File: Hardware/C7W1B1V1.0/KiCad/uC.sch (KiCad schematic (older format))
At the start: 7 parts, among them U1 STM32L082KBUx

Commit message: początkowy schemat
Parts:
- removed U1: STM32L082KBUx, Package_DFN_QFN:QFN-32-1EP_5x5mm_P0.5mm_EP3.45x3.45mm, symbol MCU_ST_STM32L0:STM32L082KBUx
- added C19: 100n/16V/X5R, Capacitor_SMD:C_0402_1005Metric, symbol Device:C
- added C5, C6: 8p/16V/C0G, Capacitor_SMD:C_0402_1005Metric, symbol Device:C
- added U1: STM32L083CZTx, Package_QFP:LQFP-48_7x7mm_P0.5mm, symbol MCU_ST_STM32L0:STM32L083CZTx
- added Y1: 830106545501, Crystal:Crystal_SMD_2012-2Pin_2.0x1.2mm, symbol Device:Crystal
- gave numbers to parts that had none: 2
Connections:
- net labels added: 5V_EN, 5V_TEST, BATT, E_INC_BUSY, E_INC_CS, E_INC_DC, E_INC_RST, MOSI, PMS_RST, PMS_TX, SCK, SCL, SDA, ~CHRG_STATUS
- wire segments 22 -> 42
- no-connect marks 0 -> 2
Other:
- moved on the sheet: C1, C2, C3, C4, R1, R2

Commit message: Dodano projekt Cube
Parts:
- renumbered C5 to C1, C6 to C2, C19 to C3, C1 to C4, C2 to C5, C3 to C6, C4 to C7, R2 to R1, R1 to R2
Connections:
- net E_INC_DC: now also U1.21 (PB10); no longer U1.39 (PB3)
- net PMS_RST: now also U1.29 (PA8)
- net PMS_TX: now also U1.31 (PA10)
- net ~CHRG_STATUS: now also U1.2 (PC13)
- net ~FLASH_CS: now reaches U1.13 (PA3)
- net ~FRAM_CS: now reaches U1.14 (PA4)
- net MISO: now reaches U1.17 (PA7)
- net PMS_SET: now reaches U1.28 (PB15)
- net PMS_RX: now reaches U1.30 (PA9)
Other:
- moved on the sheet: R1
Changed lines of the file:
@@
 	7850 950  7500 950
 $Comp
-L Device:C C4
+L Device:C C7
 U 1 1 672E6E58
 P 7500 1100
-F 0 "C4" V 7750 1050 50  0000 L CNN
+F 0 "C7" V 7750 1050 50  0000 L CNN
 F 1 "100n/16V/X5R" V 7650 650 50  0000 L CNN
 F 2 "Capacitor_SMD:C_0402_1005Metric" H 7538 950 50  0001 C CNN
@@
 	7850 950  7850 650
 $Comp
-L power:+3V3 #PWR0101
+L power:+3V3 #PWR06
 U 1 1 672E8774
 P 7850 650
-F 0 "#PWR0101" H 7850 500 50  0001 C CNN
+F 0 "#PWR06" H 7850 500 50  0001 C CNN
 F 1 "+3V3" H 7865 823 50  0000 C CNN
 F 2 "" H 7850 650 50  0001 C CNN
@@
 $EndComp
 $Comp
-L power:GND #PWR0102
+L power:GND #PWR02
 U 1 1 672E8F61
 P 6300 1250
-F 0 "#PWR0102" H 6300 1000 50  0001 C CNN
+F 0 "#PWR02" H 6300 1000 50  0001 C CNN
 F 1 "GND" H 6305 1077 50  0000 C CNN
 F 2 "" H 6300 1250 50  0001 C CNN
@@
 $EndComp
 $Comp
-L Device:C C3
+L Device:C C6
 U 1 1 672EA200
 P 7100 1100
-F 0 "C3" V 7350 1050 50  0000 L CNN
+F 0 "C6" V 7350 1050 50  0000 L CNN
 F 1 "100n/16V/X5R" V 7250 650 50  0000 L CNN
 F 2 "Capacitor_SMD:C_0402_1005Metric" H 7138 950 50  0001 C CNN
@@
 $EndComp
 $Comp
-L Device:C C2
+L Device:C C5
 U 1 1 672EA6BA
 P 6700 1100
-F 0 "C2" V 6950 1050 50  0000 L CNN
+F 0 "C5" V 6950 1050 50  0000 L CNN
 F 1 "100n/16V/X5R" V 6850 650 50  0000 L CNN
 F 2 "Capacitor_SMD:C_0402_1005Metric" H 6738 950 50  0001 C CNN
@@
 	7100 1250 6700 1250
 $Comp
-L Device:R R1
+L Device:R R2
 U 1 1 672EB48B
 P 6800 2000
-F 0 "R1" H 6870 2046 50  0000 L CNN
+F 0 "R2" H 6870 2046 50  0000 L CNN
 F 1 "10k/5%/0.063W" H 6870 1955 50  0000 L CNN
 F 2 "Resistor_SMD:R_0402_1005Metric" V 6730 2000 50  0001 C CNN
@@
 	6800 2200 6800 2150
 $Comp
-L power:+3V3 #PWR0103
+L power:+3V3 #PWR04
 U 1 1 672EC2CA
 P 6800 1850
-F 0 "#PWR0103" H 6800 1700 50  0001 C CNN
+F 0 "#PWR04" H 6800 1700 50  0001 C CNN
 F 1 "+3V3" H 6815 2023 50  0000 C CNN
 F 2 "" H 6800 1850 50  0001 C CNN
@@
 $EndComp
 $Comp
-L Device:R R2
+L Device:R R1
 U 1 1 672ECC6C
-P 6800 2650
-F 0 "R2" H 6870 2696 50  0000 L CNN
-F 1 "10k/5%/0.063W" V 6700 2600 50  0000 L CNN
-F 2 "Resistor_SMD:R_0402_1005Metric" V 6730 2650 50  0001 C CNN
-F 3 "~" H 6800 2650 50  0001 C CNN
-	1    6800 2650
-	1    0    0    -1
-$EndComp
-Wire Wire Line
-	7150 2400 6800 2400
-Wire Wire Line
-	6800 2400 6800 2500
-$Comp
-L power:GND #PWR0104
+P 6600 2500
+F 0 "R1" H 6670 2546 50  0000 L CNN
+F 1 "10k/5%/0.063W" V 6500 2450 50  0000 L CNN
+F 2 "Resistor_SMD:R_0402_1005Metric" V 6530 2500 50  0001 C CNN
+F 3 "~" H 6600 2500 50  0001 C CNN
+	1    6600 2500
+	1    0    0    -1
+$EndComp
+$Comp
+L power:GND #PWR03
 U 1 1 672ED76C
-P 6800 2800
-F 0 "#PWR0104" H 6800 2550 50  0001 C CNN
-F 1 "GND" H 6805 2627 50  0000 C CNN
-F 2 "" H 6800 2800 50  0001 C CNN
-F 3 "" H 6800 2800 50  0001 C CNN
-	1    6800 2800
-	1    0    0    -1
-$EndComp
-$Comp
-L power:GND #PWR0105
+P 6600 2650
+F 0 "#PWR03" H 6600 2400 50  0001 C CNN
+F 1 "GND" H 6605 2477 50  0000 C CNN
+F 2 "" H 6600 2650 50  0001 C CNN
+F 3 "" H 6600 2650 50  0001 C CNN
+	1    6600 2650
+	1    0    0    -1
+$EndComp
+$Comp
+L power:GND #PWR05
 U 1 1 672EDDA5
 P 7800 5100
-F 0 "#PWR0105" H 7800 4850 50  0001 C CNN
+F 0 "#PWR05" H 7800 4850 50  0001 C CNN
 F 1 "GND" H 7805 4927 50  0000 C CNN
 F 2 "" H 7800 5100 50  0001 C CNN
@@
 Text GLabel 7150 3400 0    50   Output ~ 0
 E_INC_RST
-Text GLabel 7150 3600 0    50   Output ~ 0
+Text GLabel 7150 4300 0    50   Output ~ 0
 E_INC_DC
-Text GLabel 4450 5100 2    50   Input ~ 0
+Text GLabel 8450 4100 2    50   Output ~ 0
 PMS_RST
-Text GLabel 4750 5000 0    50   Output ~ 0
+Text GLabel 8450 4300 2    50   Input ~ 0
 PMS_TX
 Text GLabel 7150 4000 0    50   BiDi ~ 0
@@
 	6700 950  6300 950
 $Comp
-L Device:C C1
+L Device:C C4
 U 1 1 672EA9E3
 P 6300 1100
-F 0 "C1" V 6550 1050 50  0000 L CNN
+F 0 "C4" V 6550 1050 50  0000 L CNN
 F 1 "100n/16V/X5R" V 6450 650 50  0000 L CNN
 F 2 "Capacitor_SMD:C_0402_1005Metric" H 6338 950 50  0001 C CNN
@@
 $EndComp
 $Comp
-L Device:C C19
+L Device:C C3
 U 1 1 67353EFC
 P 5900 1100
-F 0 "C19" V 6150 1050 50  0000 L CNN
+F 0 "C3" V 6150 1050 50  0000 L CNN
 F 1 "100n/16V/X5R" V 6050 650 50  0000 L CNN
 F 2 "Capacitor_SMD:C_0402_1005Metric" H 5938 950 50  0001 C CNN
@@
 	6000 2850 6550 2850
 $Comp
-L power:GND #PWR0106
+L power:GND #PWR01
 U 1 1 672FCAB2
 P 5100 3200
-F 0 "#PWR0106" H 5100 2950 50  0001 C CNN
+F 0 "#PWR01" H 5100 2950 50  0001 C CNN
 F 1 "GND" H 5105 3027 50  0000 C CNN
 F 2 "" H 5100 3200 50  0001 C CNN
@@
 	6000 3150 5700 3150
 $Comp
-L Device:C C6
+L Device:C C2
 U 1 1 672F9DE8
 P 5550 3150
-F 0 "C6" V 5600 3200 50  0000 L CNN
+F 0 "C2" V 5600 3200 50  0000 L CNN
 F 1 "8p/16V/C0G" V 5700 2900 50  0000 L CNN
 F 2 "Capacitor_SMD:C_0402_1005Metric" H 5588 3000 50  0001 C CNN
@@
 $EndComp
 $Comp
-L Device:C C5
+L Device:C C1
 U 1 1 672F967E
 P 5550 2850
-F 0 "C5" V 5600 2900 50  0000 L CNN
+F 0 "C1" V 5600 2900 50  0000 L CNN
 F 1 "8p/16V/C0G" V 5700 2600 50  0000 L CNN
 F 2 "Capacitor_SMD:C_0402_1005Metric" H 5588 2700 50  0001 C CNN
@@
 Text GLabel 8450 3300 2    50   Input ~ 0
 BATT
-Text GLabel 4850 6450 0    50   Output ~ 0
+Text GLabel 7150 2900 0    50   Input ~ 0
 ~CHRG_STATUS
+Text GLabel 8450 4200 2    50   Output ~ 0
+PMS_RX
+Text GLabel 7150 4800 0    50   Output ~ 0
+PMS_SET
+Wire Wire Line
+	6700 2400 6700 2350
+Wire Wire Line
+	6700 2350 6600 2350
+Wire Wire Line
+	6700 2400 7150 2400
+Text GLabel 8450 4000 2    50   Input ~ 0
+MISO
+Text GLabel 8450 3600 2    50   Input ~ 0
+~FLASH_CS
+Text GLabel 8450 3700 2    50   Input ~ 0
+~FRAM_CS
 $EndSCHEMATC

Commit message: Ukończono PCB. dodano pliki produkcyjne
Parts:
- added J5: Conn_01x07, Connector_PinSocket_2.54mm:PinSocket_1x07_P2.54mm_Vertical, symbol Connector_Generic:Conn_01x07
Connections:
- net 5V_EN: now also U1.11 (PA1); no longer U1.12 (PA2)
- net 5V_TEST: now also U1.12 (PA2); no longer U1.11 (PA1)
- net GND: now also J5.6 (Pin_6), J5.7 (Pin_7)
- net RST: now reaches R2.2, U1.7 (NRST)
- net RST: now also J5.1 (Pin_1)
- net USB_D-: now reaches U1.32 (PA11)
- net USB_D+: now reaches U1.33 (PA12)
- net SWDIO: now reaches U1.34 (PA13)
- net SWDIO: now also J5.5 (Pin_5)
- net SWCLK: now reaches U1.37 (PA14)
- net SWCLK: now also J5.4 (Pin_4)
- net TX: now reaches U1.39 (PB3)
- net TX: now also J5.3 (Pin_3)
- net RX: now reaches U1.40 (PB4)
- net RX: now also J5.2 (Pin_2)
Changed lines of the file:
@@
 NoConn ~ 7150 2600
 NoConn ~ 7150 2700
+Text GLabel 8450 3400 2    50   Output ~ 0
+5V_EN
 Text GLabel 8450 3500 2    50   Output ~ 0
-5V_EN
-Text GLabel 8450 3400 2    50   Output ~ 0
 5V_TEST
 Text GLabel 8450 3300 2    50   Input ~ 0
@@
 Text GLabel 8450 3700 2    50   Input ~ 0
 ~FRAM_CS
+Text GLabel 8450 4500 2    50   BiDi ~ 0
+USB_D+
+Text GLabel 8450 4400 2    50   BiDi ~ 0
+USB_D-
+Text GLabel 8450 4700 2    50   Input ~ 0
+SWCLK
+Text GLabel 8450 4600 2    50   BiDi ~ 0
+SWDIO
+Text GLabel 7150 3600 0    50   Output ~ 0
+TX
+Text GLabel 7150 3700 0    50   Input ~ 0
+RX
+Text GLabel 9950 1200 3    50   Input ~ 0
+TX
+Text GLabel 9850 1200 3    50   Output ~ 0
+RX
+Text GLabel 10050 1200 3    50   Output ~ 0
+SWCLK
+Text GLabel 10150 1200 3    50   BiDi ~ 0
+SWDIO
+Text GLabel 6800 2200 0    50   Input ~ 0
+RST
+Text GLabel 9750 1200 3    50   Output ~ 0
+RST
+$Comp
+L power:GND #PWR0108
+U 1 1 6753B37F
+P 10300 1300
+F 0 "#PWR0108" H 10300 1050 50  0001 C CNN
+F 1 "GND" H 10305 1127 50  0000 C CNN
+F 2 "" H 10300 1300 50  0001 C CNN
+F 3 "" H 10300 1300 50  0001 C CNN
+	1    10300 1300
+	1    0    0    -1
+$EndComp
+$Comp
+L Connector_Generic:Conn_01x07 J5
+U 1 1 6753EA67
+P 10050 1000
+F 0 "J5" V 10014 612 50  0000 R CNN
+F 1 "Conn_01x07" V 9923 612 50  0000 R CNN
+F 2 "Connector_PinSocket_2.54mm:PinSocket_1x07_P2.54mm_Vertical" H 10050 1000 50  0001 C CNN
+F 3 "~" H 10050 1000 50  0001 C CNN
+	1    10050 1000
+	0    -1   -1   0
+$EndComp
+Wire Wire Line
+	10250 1200 10300 1200
+Wire Wire Line
+	10300 1200 10300 1300
+Connection ~ 10300 1200
+Wire Wire Line
+	10300 1200 10350 1200
 $EndSCHEMATC

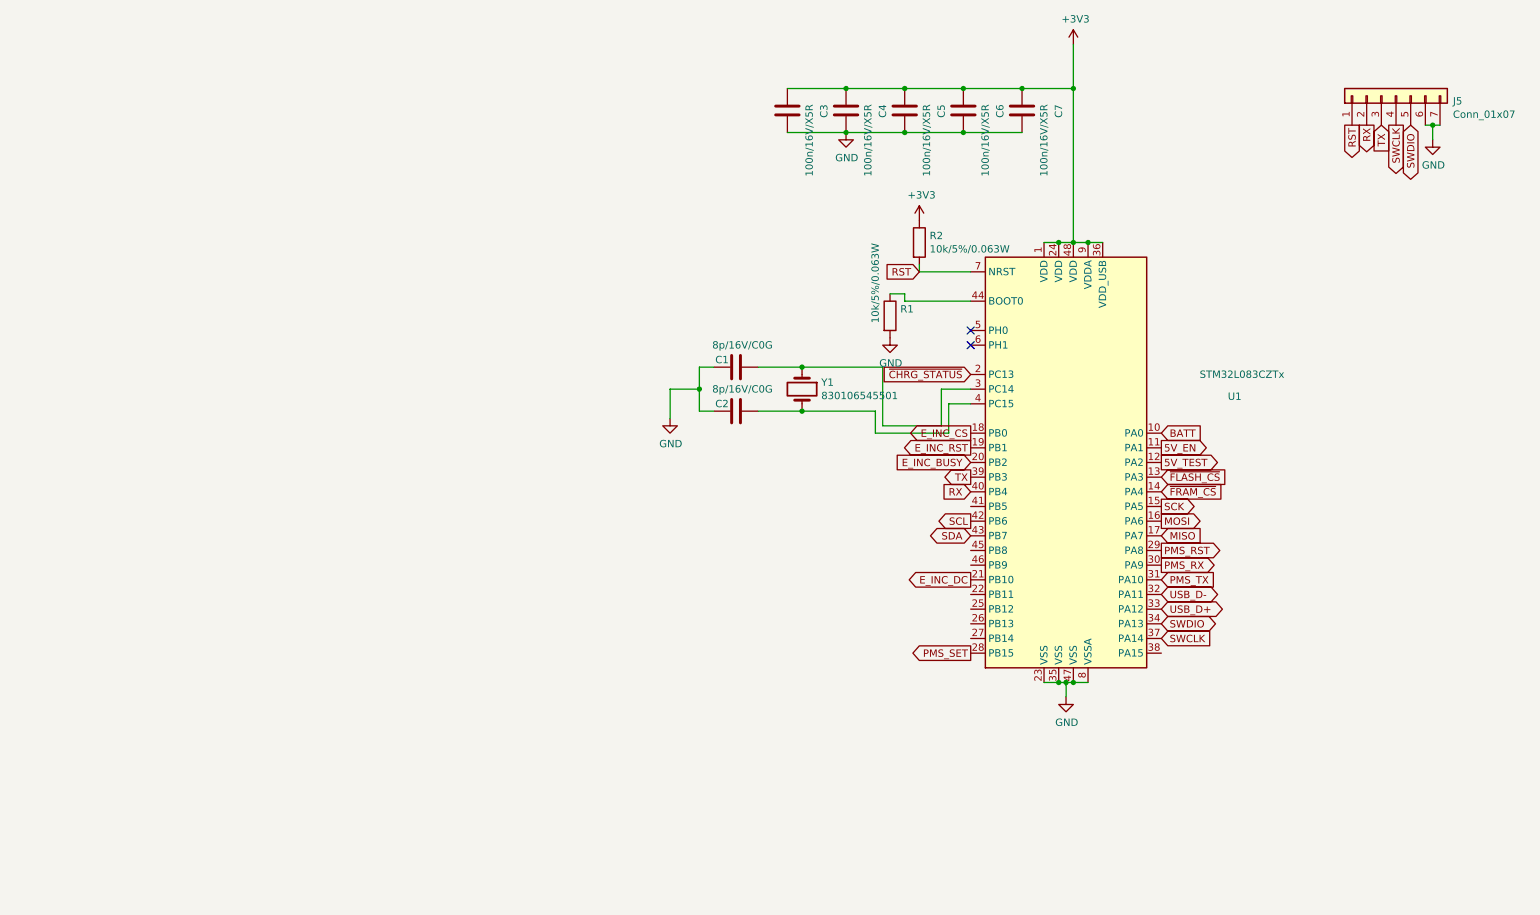
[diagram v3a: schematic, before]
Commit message: Zmieniono procesor na wersję LQFP-64
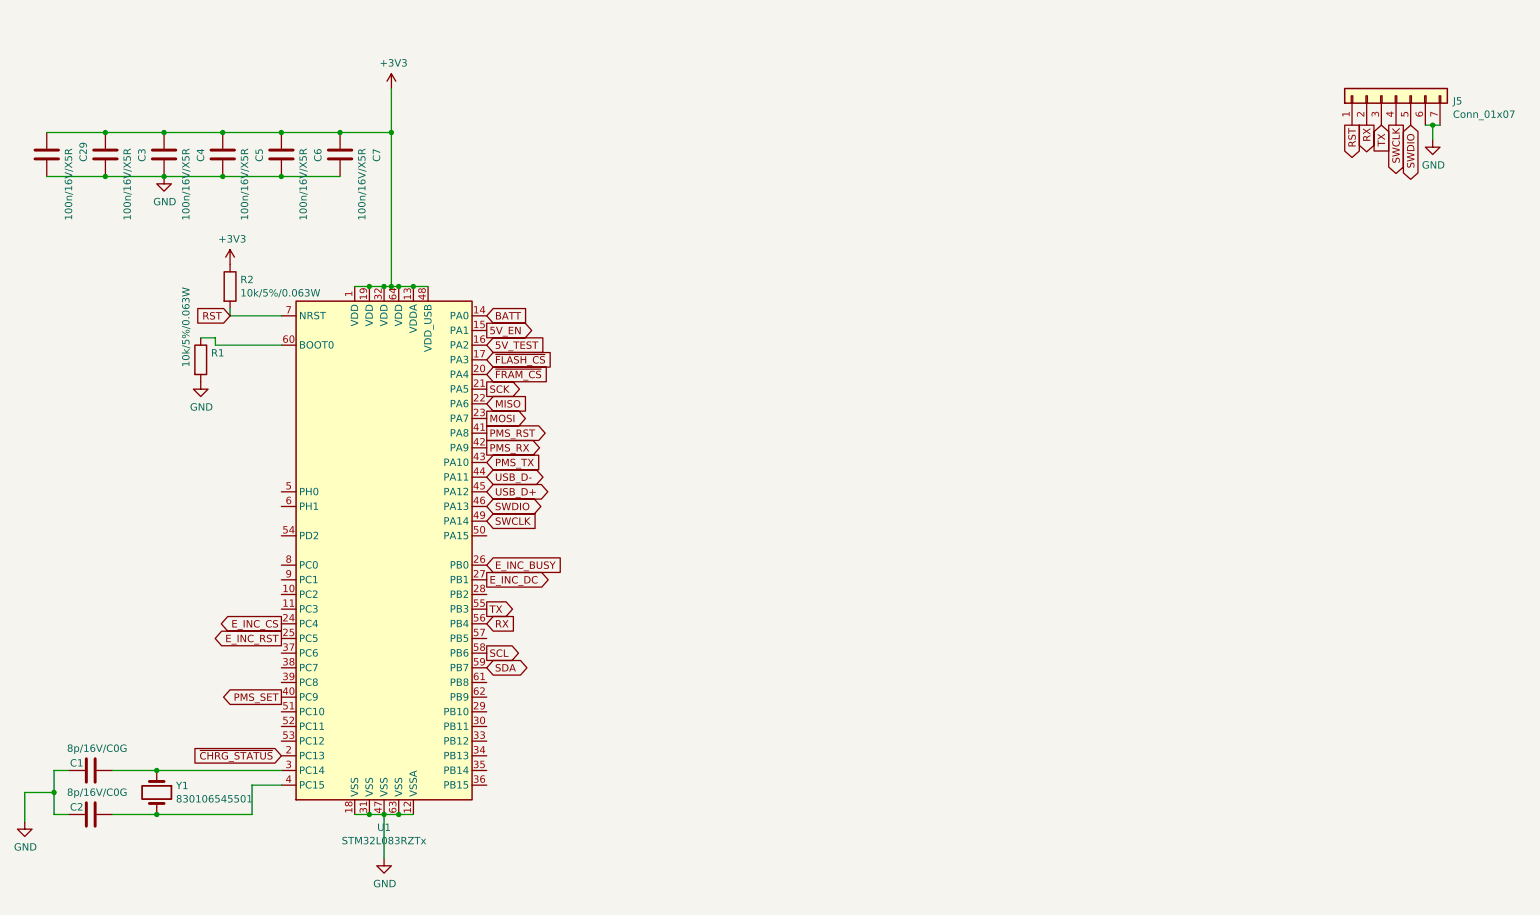
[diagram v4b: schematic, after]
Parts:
- removed U1: STM32L083CZTx, Package_QFP:LQFP-48_7x7mm_P0.5mm, symbol MCU_ST_STM32L0:STM32L083CZTx
- added C29: 100n/16V/X5R, Capacitor_SMD:C_0402_1005Metric, symbol Device:C
- added U1: STM32L083RZTx, Package_QFP:LQFP-64_10x10mm_P0.5mm, symbol MCU_ST_STM32L0:STM32L083RZTx
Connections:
- net +3V3: now also C29.1, U1.1 (VDD), U1.13 (VDDA), U1.19 (VDD), U1.32 (VDD), U1.48 (VDD_USB), U1.64 (VDD)
- net 5V_EN: now also U1.15 (PA1)
- net 5V_TEST: now also U1.16 (PA2)
- net BATT: now also U1.14 (PA0)
- net E_INC_BUSY: now also U1.26 (PB0)
- net E_INC_CS: now also U1.24 (PC4)
- net E_INC_DC: now also U1.27 (PB1)
- net E_INC_RST: now also U1.25 (PC5)
- net GND: now also C29.2, U1.12 (VSSA), U1.18 (VSS), U1.31 (VSS), U1.47 (VSS), U1.63 (VSS)
- net MISO: now also U1.22 (PA6)
- net MOSI: now also U1.23 (PA7)
- net PMS_RST: now also U1.41 (PA8)
- net PMS_RX: now also U1.42 (PA9)
- net PMS_SET: now also U1.40 (PC9)
- net PMS_TX: now also U1.43 (PA10)
- net RST: now also U1.7 (NRST)
- net RX: now also U1.56 (PB4)
- net SCK: now also U1.21 (PA5)
- net SCL: now also U1.58 (PB6)
- net SDA: now also U1.59 (PB7)
- net SWCLK: now also U1.49 (PA14)
- net SWDIO: now also U1.46 (PA13)
- net TX: now also U1.55 (PB3)
- net USB_D+: now also U1.45 (PA12)
- net USB_D-: now also U1.44 (PA11)
- net ~CHRG_STATUS: now also U1.2 (PC13)
- net ~FLASH_CS: now also U1.17 (PA3)
- net ~FRAM_CS: now also U1.20 (PA4)
- net at R1.1: now also U1.60 (BOOT0)
- net at C1.2, Y1.1: now also U1.3 (PC14)
- net at C2.2, Y1.2: now also U1.4 (PC15)
- no-connect marks 2 -> 0
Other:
- moved on the sheet: C1, C2, C3, C4, C5, C6, C7, R1, R2, Y1
